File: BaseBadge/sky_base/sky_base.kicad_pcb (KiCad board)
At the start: 2 copper layers, 107.2 x 43.8 mm, 13 parts, among them J1 Conn_02x03_Counter_Clockwise, J2 Conn_02x03_Counter_Clockwise

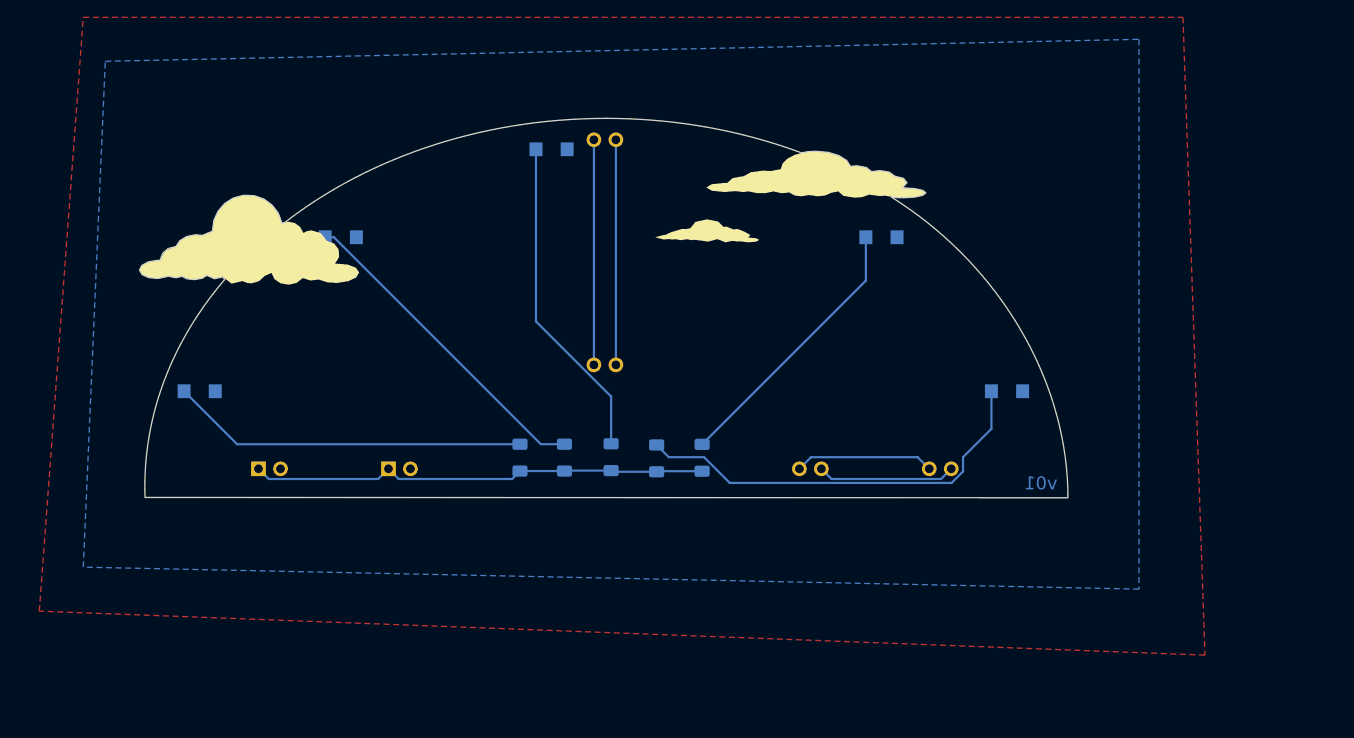
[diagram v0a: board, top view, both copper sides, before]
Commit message: overhauls across boards to v02
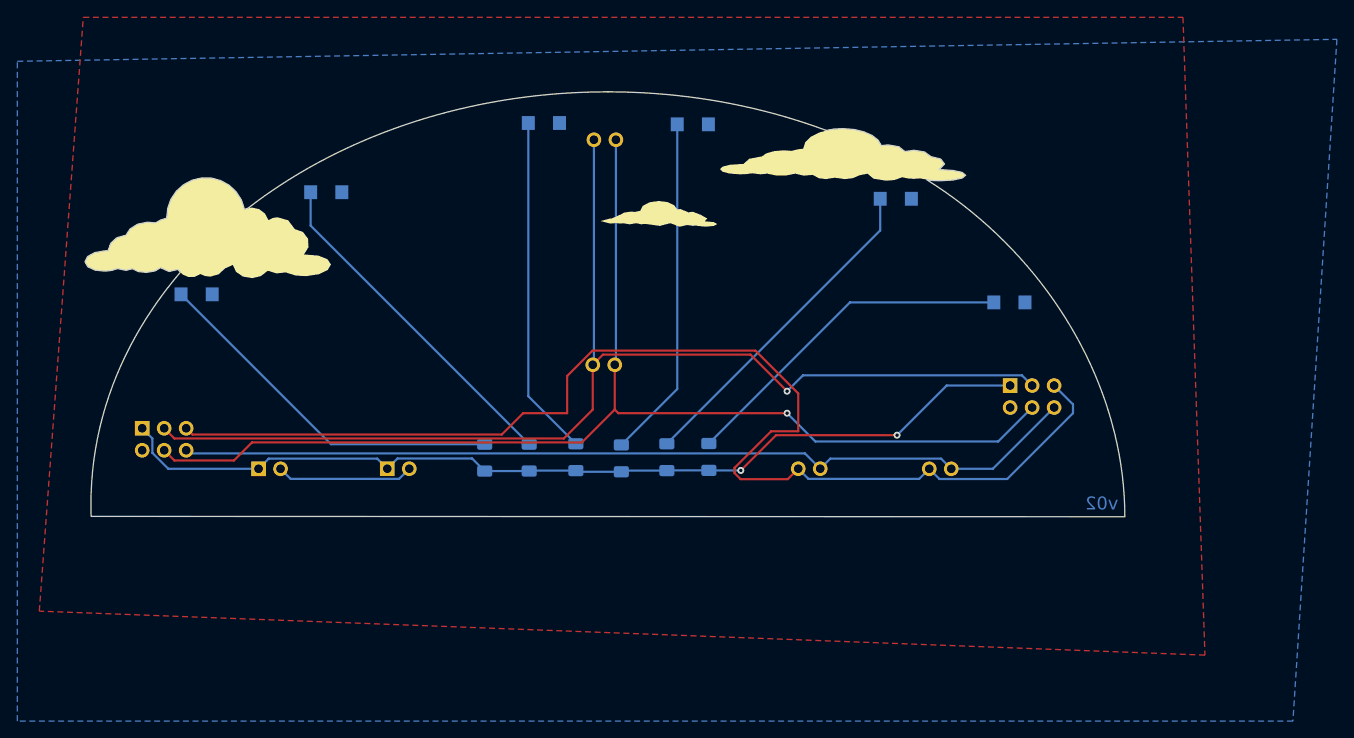
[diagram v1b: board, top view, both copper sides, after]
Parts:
- removed the svg2mod at (149.9, 101.6)
- added D6: LED, Base_Library:APTR3216-VFX, B.Cu at (195.9, 96.4)
- added J3: Conn_02x03_Counter_Clockwise, Connector_PinHeader_2.54mm:PinHeader_2x03_P2.54mm_Vertical, B.Cu at (95.7, 111.0)
- added J4: Conn_02x03_Counter_Clockwise, Base_Library:sky2ground_connector, F.Cu at (149.0, 115.6)
- added R6: 330, Resistor_SMD:R_1206_3216Metric_Pad1.30x1.75mm_HandSolder, B.Cu at (161.1, 114.3)
- added svg2mod: G***, aerospace_badge:sky_base, F.Cu at (146.1, 105.7)
- D1, D2, D3, D4, D5: footprint SpaceBase_Library:APTR3216-VFX -> Base_Library:APTR3216-VFX
- J1: footprint SpaceBase_Library:space2sky_connector -> Connector_PinHeader_2.54mm:PinHeader_2x03_P2.54mm_Vertical; moved to B.Cu
- J2: footprint SpaceBase_Library:spaceBase_connector -> Base_Library:space2sky_connector
- moved J1 47.8 mm to (195.9, 106.0), turned to -90 degrees
- moved D4 47.6 mm to (159.3, 75.9)
- moved D1 11.2 mm to (102.0, 95.5)
- moved D2 5.47 mm to (117.0, 83.7)
- moved D5 4.74 mm to (182.7, 84.5)
- moved R5 4.08 mm to (156.3, 114.3)
- moved R1 4.08 mm to (135.3, 114.4)
- moved R2 4.08 mm to (140.4, 114.3)
- moved R3 4.08 mm to (145.8, 114.3)
- moved R4 4.08 mm to (151.0, 114.4)
- moved D3 3.16 mm to (142.1, 75.7)
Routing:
- net Net-(J1-Pad5): track 16.1 -> 142.2 mm
- net Net-(J1-Pad4): track 26.0 -> 137.5 mm, vias 0 -> 1
- net Net-(J2-Pad3): track 26.0 -> 136.8 mm, vias 0 -> 1
- net Net-(J1-Pad6): track 16.0 -> 105.0 mm
- net VCC: track 53.2 -> 109.4 mm, vias 0 -> 2
- net Net-(D6-Pad2): track 0.00 -> 39.7 mm
- net GND: track 0.00 -> 15.8 mm
- net Net-(D4-Pad2): track 48.4 -> 39.7 mm
- net Net-(D5-Pad2): track 31.8 -> 38.5 mm
- net Net-(D2-Pad2): track 37.5 -> 39.6 mm
- net Net-(D3-Pad2): track 37.6 -> 39.3 mm
- net Net-(D1-Pad2): track 41.3 -> 42.2 mm
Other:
- board size 107.2 x 43.8 mm -> 120.1 x 49.1 mm
- board text added: "v02"
- board text removed: "v01"
